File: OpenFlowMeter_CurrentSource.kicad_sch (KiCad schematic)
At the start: 20 parts, among them J1 Screw_Terminal_01x02, Q1 BC856, U1 LT1492

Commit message: BUGFIX footprint of LT1490
Footprint of LT1490 is SOIC8 and not Micro 8 -> had to enlarge the board.
At the same step, changed all footprints from handsolder to normal solder. (saves a little space)
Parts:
- C1, C2: footprint Capacitor_SMD:C_0603_1608Metric_Pad1.08x0.95mm_HandSolder -> Capacitor_SMD:C_0603_1608Metric
- R1, R10, R11, R12, R2, R27, R3, R4, R5, R6, R7, R9: footprint Resistor_SMD:R_0603_1608Metric_Pad0.98x0.95mm_HandSolder -> Resistor_SMD:R_0603_1608Metric
- U1: footprint Package_SO:OnSemi_Micro8 -> Package_SO:SOIC-8_3.9x4.9mm_P1.27mm
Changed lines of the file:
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@@
     (property "Reference" "U1" (id 0) (at 90.17 93.1418 0))
     (property "Value" "LT1492" (id 1) (at 90.17 90.8304 0))
-    (property "Footprint" "Package_SO:OnSemi_Micro8" (id 2) (at 90.17 83.82 0)
+    (property "Footprint" "Package_SO:SOIC-8_3.9x4.9mm_P1.27mm" (id 2) (at 90.17 83.82 0)
       (effects (font (size 1.27 1.27)) hide)
     )
@@
     (property "Reference" "U1" (id 0) (at 172.72 106.2482 0))
     (property "Value" "LT1492" (id 1) (at 172.72 108.5596 0))
-    (property "Footprint" "Package_SO:OnSemi_Micro8" (id 2) (at 172.72 115.57 0)
+    (property "Footprint" "Package_SO:SOIC-8_3.9x4.9mm_P1.27mm" (id 2) (at 172.72 115.57 0)
       (effects (font (size 1.27 1.27)) hide)
     )
@@
       (effects (font (size 1.27 1.27)) (justify left))
     )
-    (property "Footprint" "Package_SO:OnSemi_Micro8" (id 2) (at 167.64 63.5 0)
+    (property "Footprint" "Package_SO:SOIC-8_3.9x4.9mm_P1.27mm" (id 2) (at 167.64 63.5 0)
       (effects (font (size 1.27 1.27)) hide)
     )
@@
     (property "Reference" "R1" (id 0) (at 50.8 76.0222 90))
     (property "Value" "1k" (id 1) (at 50.8 78.3336 90))
-    (property "Footprint" "Resistor_SMD:R_0603_1608Metric_Pad0.98x0.95mm_HandSolder" (id 2) (at 50.8 79.502 90)
+    (property "Footprint" "Resistor_SMD:R_0603_1608Metric" (id 2) (at 50.8 79.502 90)
       (effects (font (size 1.27 1.27)) hide)
     )
@@
     (property "Reference" "R4" (id 0) (at 102.87 124.2822 90))
     (property "Value" "47k" (id 1) (at 102.87 126.5936 90))
-    (property "Footprint" "Resistor_SMD:R_0603_1608Metric_Pad0.98x0.95mm_HandSolder" (id 2) (at 102.87 127.762 90)
+    (property "Footprint" "Resistor_SMD:R_0603_1608Metric" (id 2) (at 102.87 127.762 90)
       (effects (font (size 1.27 1.27)) hide)
     )
@@
       (effects (font (size 1.27 1.27)) (justify left))
     )
-    (property "Footprint" "Resistor_SMD:R_0603_1608Metric_Pad0.98x0.95mm_HandSolder" (id 2) (at 116.332 72.39 90)
+    (property "Footprint" "Resistor_SMD:R_0603_1608Metric" (id 2) (at 116.332 72.39 90)
       (effects (font (size 1.27 1.27)) hide)
     )
@@
     (property "Reference" "R5" (id 0) (at 104.14 78.5622 90))
     (property "Value" "100" (id 1) (at 104.14 80.8736 90))
-    (property "Footprint" "Resistor_SMD:R_0603_1608Metric_Pad0.98x0.95mm_HandSolder" (id 2) (at 104.14 82.042 90)
+    (property "Footprint" "Resistor_SMD:R_0603_1608Metric" (id 2) (at 104.14 82.042 90)
       (effects (font (size 1.27 1.27)) hide)
     )
@@
       (effects (font (size 1.27 1.27)) (justify left))
     )
-    (property "Footprint" "Resistor_SMD:R_0603_1608Metric_Pad0.98x0.95mm_HandSolder" (id 2) (at 116.332 115.57 90)
+    (property "Footprint" "Resistor_SMD:R_0603_1608Metric" (id 2) (at 116.332 115.57 90)
       (effects (font (size 1.27 1.27)) hide)
     )
@@
     (property "Reference" "R3" (id 0) (at 102.87 96.3422 90))
     (property "Value" "47k" (id 1) (at 102.87 98.6536 90))
-    (property "Footprint" "Resistor_SMD:R_0603_1608Metric_Pad0.98x0.95mm_HandSolder" (id 2) (at 102.87 99.822 90)
+    (property "Footprint" "Resistor_SMD:R_0603_1608Metric" (id 2) (at 102.87 99.822 90)
       (effects (font (size 1.27 1.27)) hide)
     )
@@
     (property "Reference" "R2" (id 0) (at 74.93 96.3422 90))
     (property "Value" "47k" (id 1) (at 74.93 98.6536 90))
-    (property "Footprint" "Resistor_SMD:R_0603_1608Metric_Pad0.98x0.95mm_HandSolder" (id 2) (at 74.93 99.822 90)
+    (property "Footprint" "Resistor_SMD:R_0603_1608Metric" (id 2) (at 74.93 99.822 90)
       (effects (font (size 1.27 1.27)) hide)
     )
@@
     (property "Reference" "R9" (id 0) (at 152.4 96.3422 90))
     (property "Value" "22k" (id 1) (at 152.4 98.6536 90))
-    (property "Footprint" "Resistor_SMD:R_0603_1608Metric_Pad0.98x0.95mm_HandSolder" (id 2) (at 152.4 99.822 90)
+    (property "Footprint" "Resistor_SMD:R_0603_1608Metric" (id 2) (at 152.4 99.822 90)
       (effects (font (size 1.27 1.27)) hide)
     )
@@
     (property "Reference" "R10" (id 0) (at 152.4 124.2822 90))
     (property "Value" "22k" (id 1) (at 152.4 126.5936 90))
-    (property "Footprint" "Resistor_SMD:R_0603_1608Metric_Pad0.98x0.95mm_HandSolder" (id 2) (at 152.4 127.762 90)
+    (property "Footprint" "Resistor_SMD:R_0603_1608Metric" (id 2) (at 152.4 127.762 90)
       (effects (font (size 1.27 1.27)) hide)
     )
@@
     (property "Reference" "R11" (id 0) (at 171.45 96.3422 90))
     (property "Value" "10k" (id 1) (at 171.45 98.6536 90))
-    (property "Footprint" "Resistor_SMD:R_0603_1608Metric_Pad0.98x0.95mm_HandSolder" (id 2) (at 171.45 99.822 90)
+    (property "Footprint" "Resistor_SMD:R_0603_1608Metric" (id 2) (at 171.45 99.822 90)
       (effects (font (size 1.27 1.27)) hide)
     )
@@
     (property "Reference" "R12" (id 0) (at 171.45 124.2822 90))
     (property "Value" "10k" (id 1) (at 171.45 126.5936 90))
-    (property "Footprint" "Resistor_SMD:R_0603_1608Metric_Pad0.98x0.95mm_HandSolder" (id 2) (at 171.45 127.762 90)
+    (property "Footprint" "Resistor_SMD:R_0603_1608Metric" (id 2) (at 171.45 127.762 90)
       (effects (font (size 1.27 1.27)) hide)
     )
@@
     (property "Reference" "R27" (id 0) (at 134.62 136.9822 90))
     (property "Value" "1k" (id 1) (at 134.62 139.2936 90))
-    (property "Footprint" "Resistor_SMD:R_0603_1608Metric_Pad0.98x0.95mm_HandSolder" (id 2) (at 134.62 140.462 90)
+    (property "Footprint" "Resistor_SMD:R_0603_1608Metric" (id 2) (at 134.62 140.462 90)
       (effects (font (size 1.27 1.27)) hide)
     )
@@
       (effects (font (size 1.27 1.27)) (justify left))
     )
-    (property "Footprint" "Capacitor_SMD:C_0603_1608Metric_Pad1.08x0.95mm_HandSolder" (id 2) (at 180.0352 67.31 0)
+    (property "Footprint" "Capacitor_SMD:C_0603_1608Metric" (id 2) (at 180.0352 67.31 0)
       (effects (font (size 1.27 1.27)) hide)
     )
@@
       (effects (font (size 1.27 1.27)) (justify left))
     )
-    (property "Footprint" "Capacitor_SMD:C_0603_1608Metric_Pad1.08x0.95mm_HandSolder" (id 2) (at 128.27 65.0748 0)
-      (effects (font (size 1.27 1.27)) hide)
-    )
+    (property "Footprint" "Capacitor_SMD:C_0603_1608Metric" (id 2) (at 128.27 65.0748 0)
+      (effects (font (size 1.27 1.27)) hide)
+    )

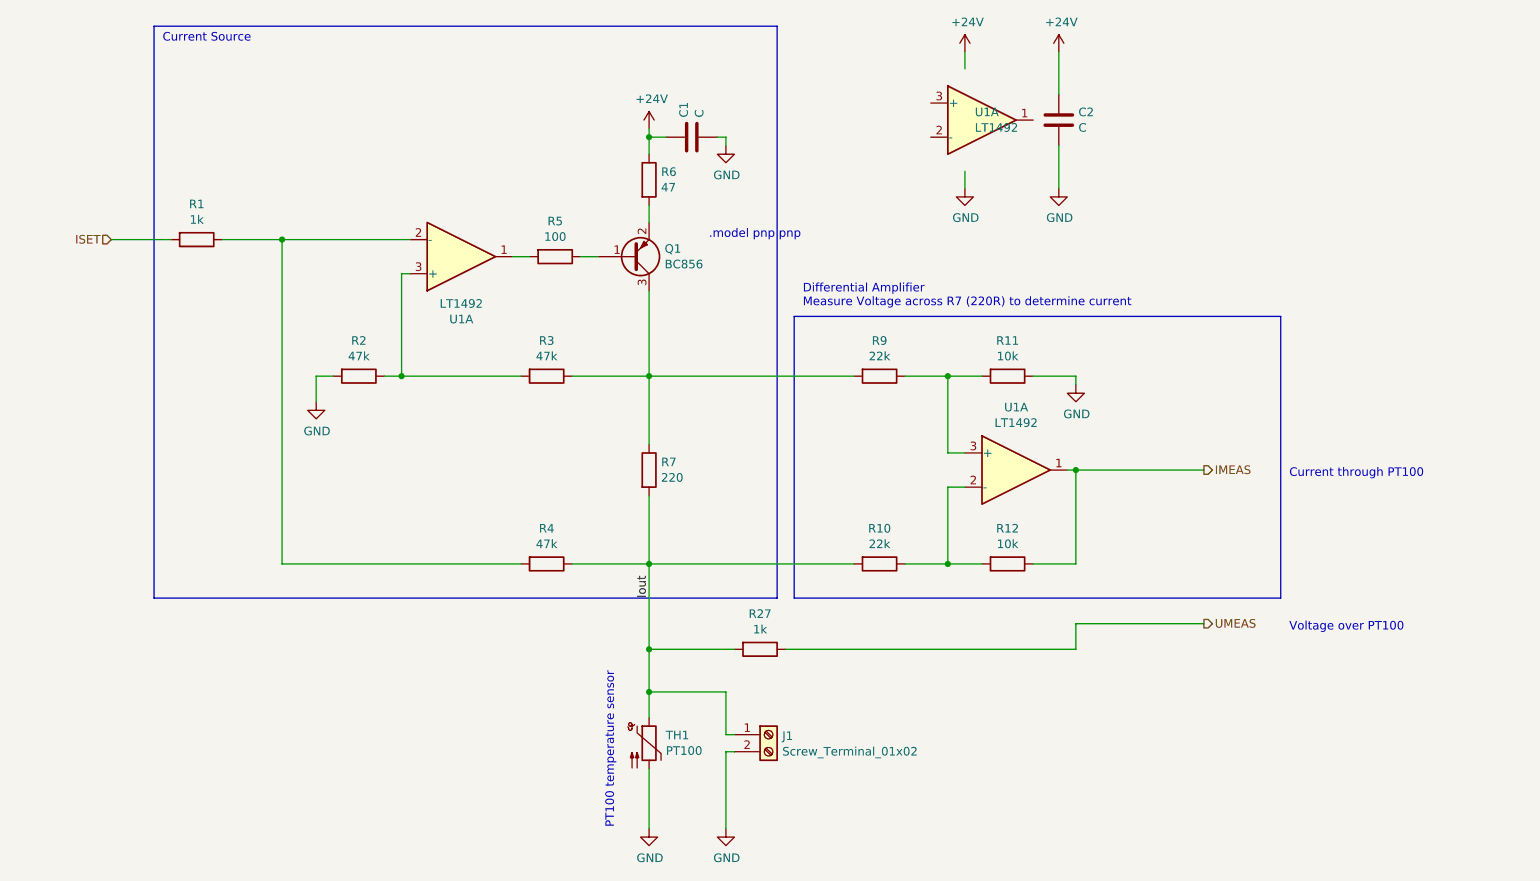
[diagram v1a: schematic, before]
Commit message: added ADC protection
added Zener diodes as ADC input protection in combination with current limiting resistors.
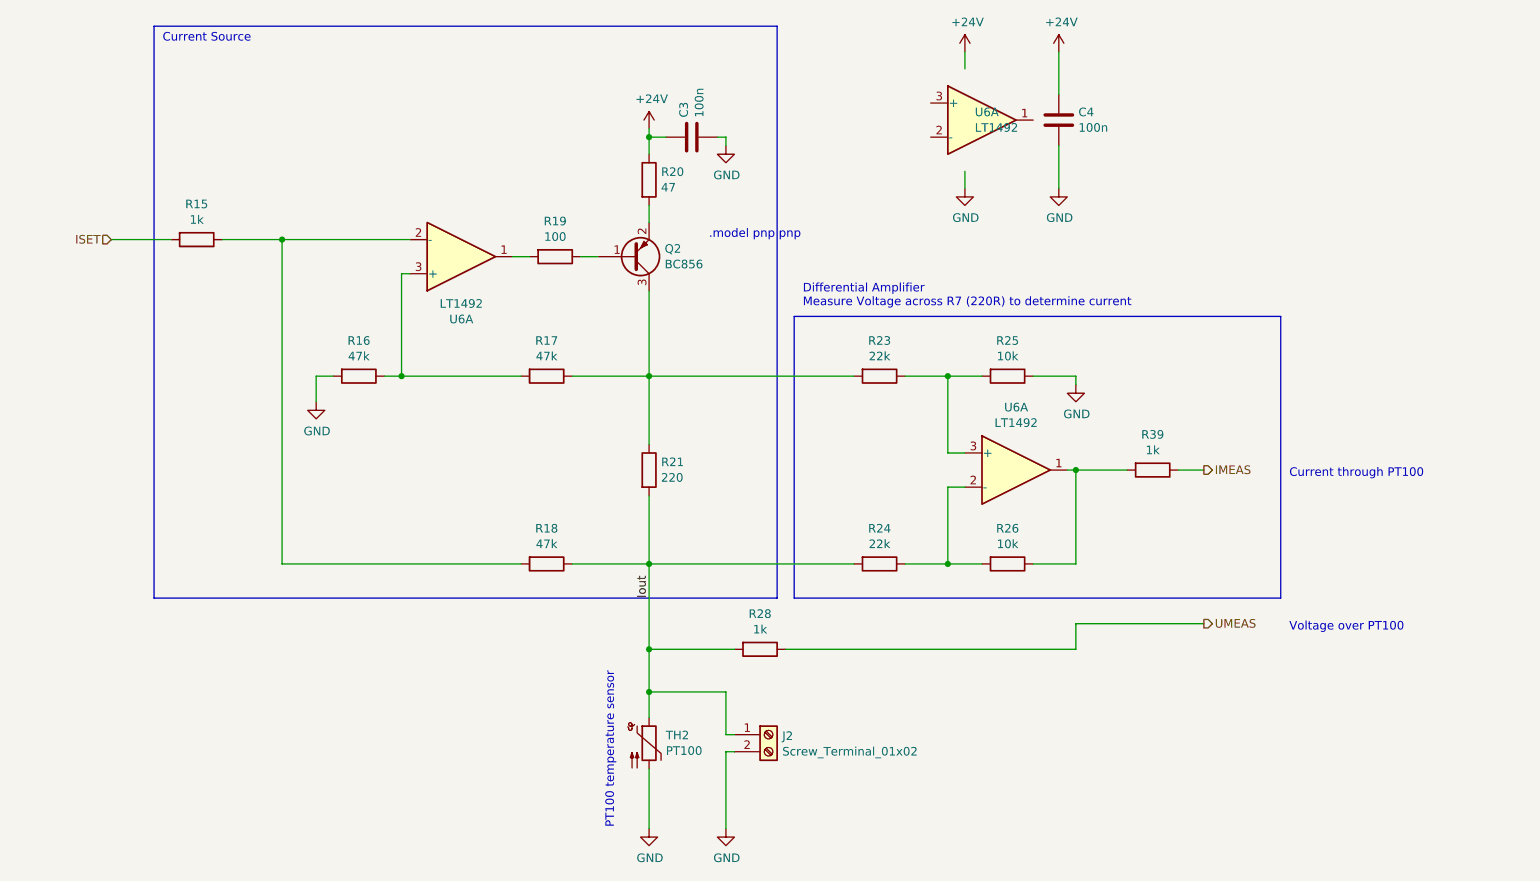
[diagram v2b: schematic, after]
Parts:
- added R39: 1k, Resistor_SMD:R_0603_1608Metric, symbol Device:R
- C3: renamed from C1; value C -> 100n
- C4: renamed from C2; value C -> 100n
- renumbered J1 to J2, Q1 to Q2, R1 to R15, R2 to R16, R3 to R17, R4 to R18, R5 to R19, R6 to R20, R7 to R21, R9 to R23, R10 to R24, R11 to R25, R12 to R26, R27 to R28, TH1 to TH2, U1 to U6
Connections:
- net IMEAS: now also R39.1; no longer R26.1, U6.1
- new net: R26.1, R39.2, U6.1
